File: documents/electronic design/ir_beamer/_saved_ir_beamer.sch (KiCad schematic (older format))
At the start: 42 parts, among them P1 Via, P10 Via, P2 Via, P3 Via, P4 Via, P5 Via, P7 Via, P8 Via, P9 Via, T1 2N7002K, T10 2N7002K, T11 2N7002K, T12 2N7002K, T2 2N7002K, T3 2N7002K, T4 2N7002K, T5 2N7002K, T6 2N7002K, T7 2N7002K, T8 2N7002K, T9 2N7002K, U1 74HC595D, U2 STM32F103HEADER, U3 74HC595D, U4 SE8R01_module

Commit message: update pcb for beamer (use 5V to drive LED)
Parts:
- R5: footprint (none) -> Resistors_SMD:R_0805_HandSoldering
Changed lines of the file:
@@
 F 0 "R5" V 4330 4650 50  0000 C CNN
 F 1 "100" V 4250 4650 50  0000 C CNN
-F 2 "" V 4180 4650 50  0000 C CNN
+F 2 "Resistors_SMD:R_0805_HandSoldering" V 4180 4650 50  0001 C CNN
 F 3 "" H 4250 4650 50  0000 C CNN
 	1    4250 4650

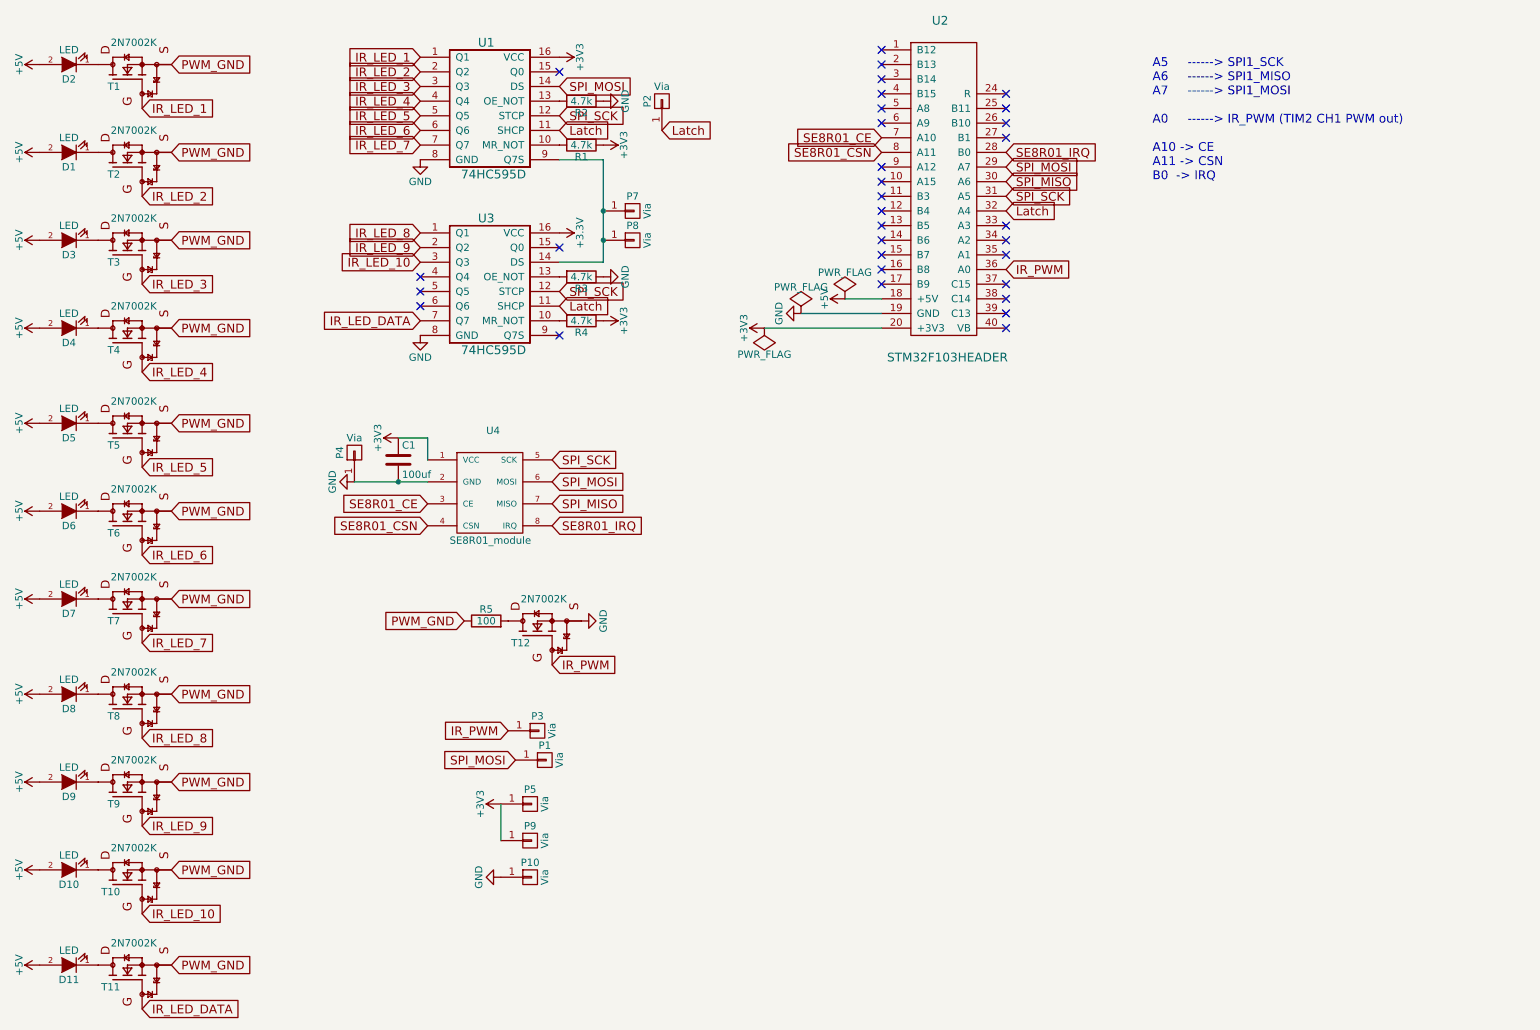
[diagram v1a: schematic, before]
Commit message: update PCB projects for beamer and sensor
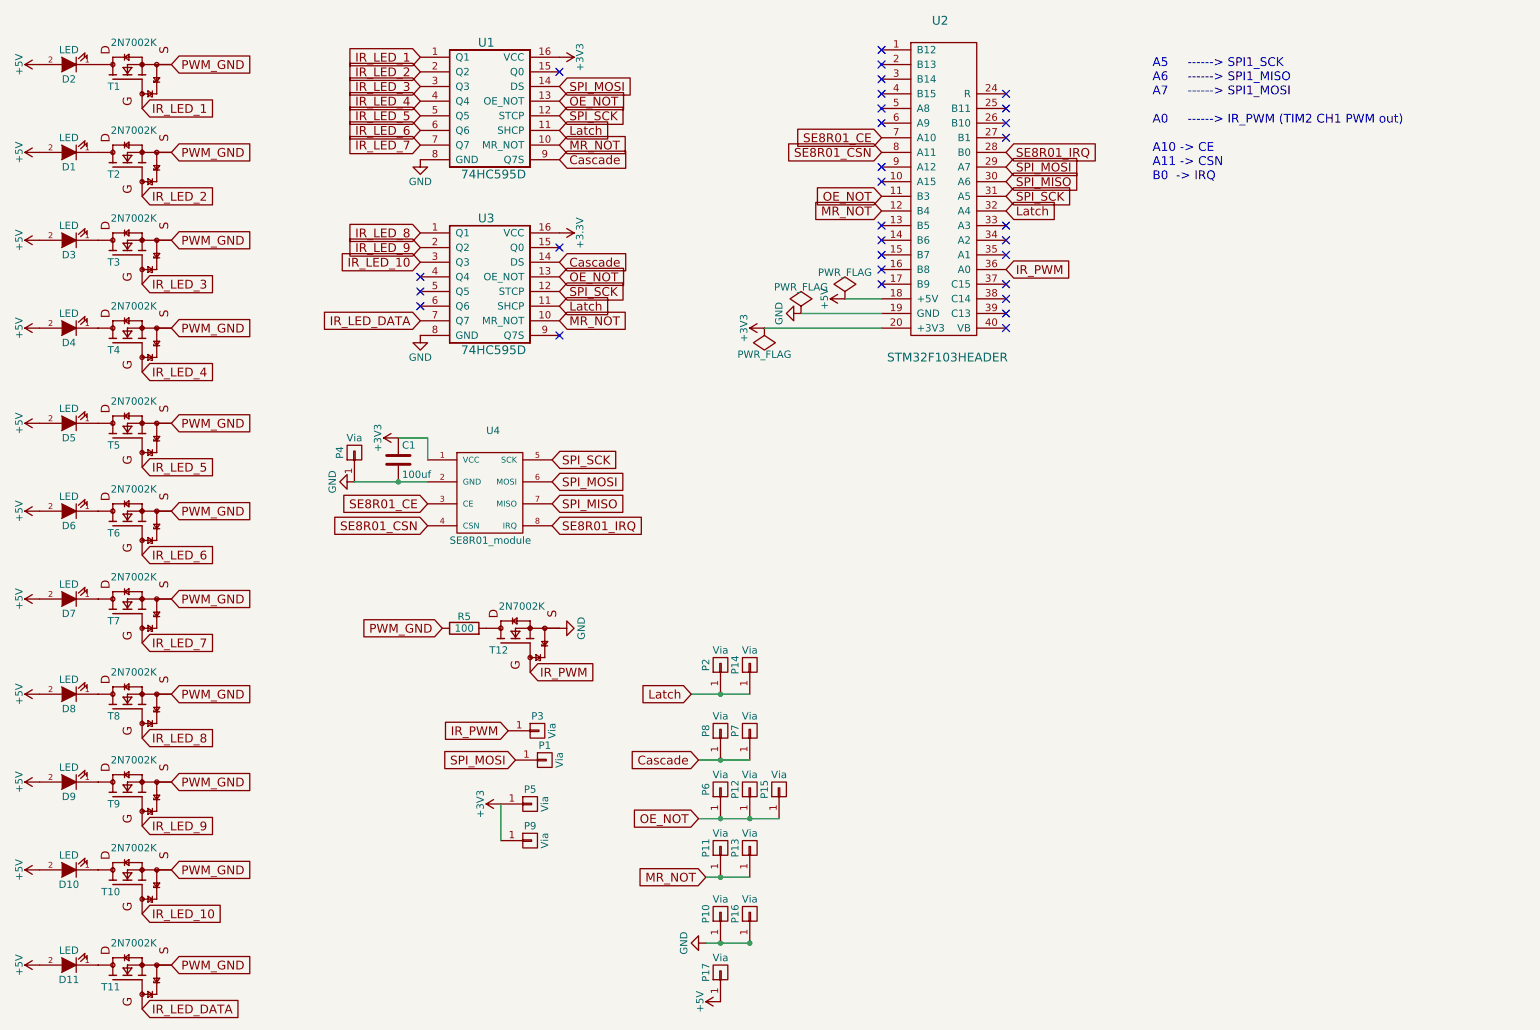
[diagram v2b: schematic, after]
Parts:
- removed R1, R2, R3, R4: 4.7k, Resistors_SMD:R_0805_HandSoldering, symbol R
- added P11, P12, P13, P14, P15, P16, P17, P6: Via, footprints:Via, symbol Via
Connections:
- net +5V: now also P17.1 (P1)
- net GND: now also P16.1 (P1)
- net Latch: now also P14.1 (P1)
- net MR_NOT: now reaches U1.10 (MR_NOT)
- net MR_NOT: now also U2.12 (B4), U3.10 (MR_NOT), P11.1 (P1), P13.1 (P1)
- net OE_NOT: now reaches U1.13 (OE_NOT)
- net OE_NOT: now also U2.11 (B3), U3.13 (OE_NOT), P12.1 (P1), P15.1 (P1), P6.1 (P1)
- net Cascade: now reaches P7.1 (P1), P8.1 (P1), U1.9 (Q7S), U3.14 (DS)
- no-connect marks 32 -> 30
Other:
- moved on the sheet: P10, P2, P7, P8, R5, T12
